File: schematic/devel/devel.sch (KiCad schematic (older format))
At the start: 61 parts, among them J1 CONN_PWR, J2 CONN_X1, J3 CONN_Y2, J4 CONN_X2, J5 CONN_Y1, Q1 Q_PMOS_GSD, Q2 Q_NMOS_GSD, Q3 Q_PMOS_GSD, Q4 Q_NMOS_GSD, U1 LM317_SOT223, U2 LM337_SOT223, U3 REF5010IDGK, U4 OPA4197

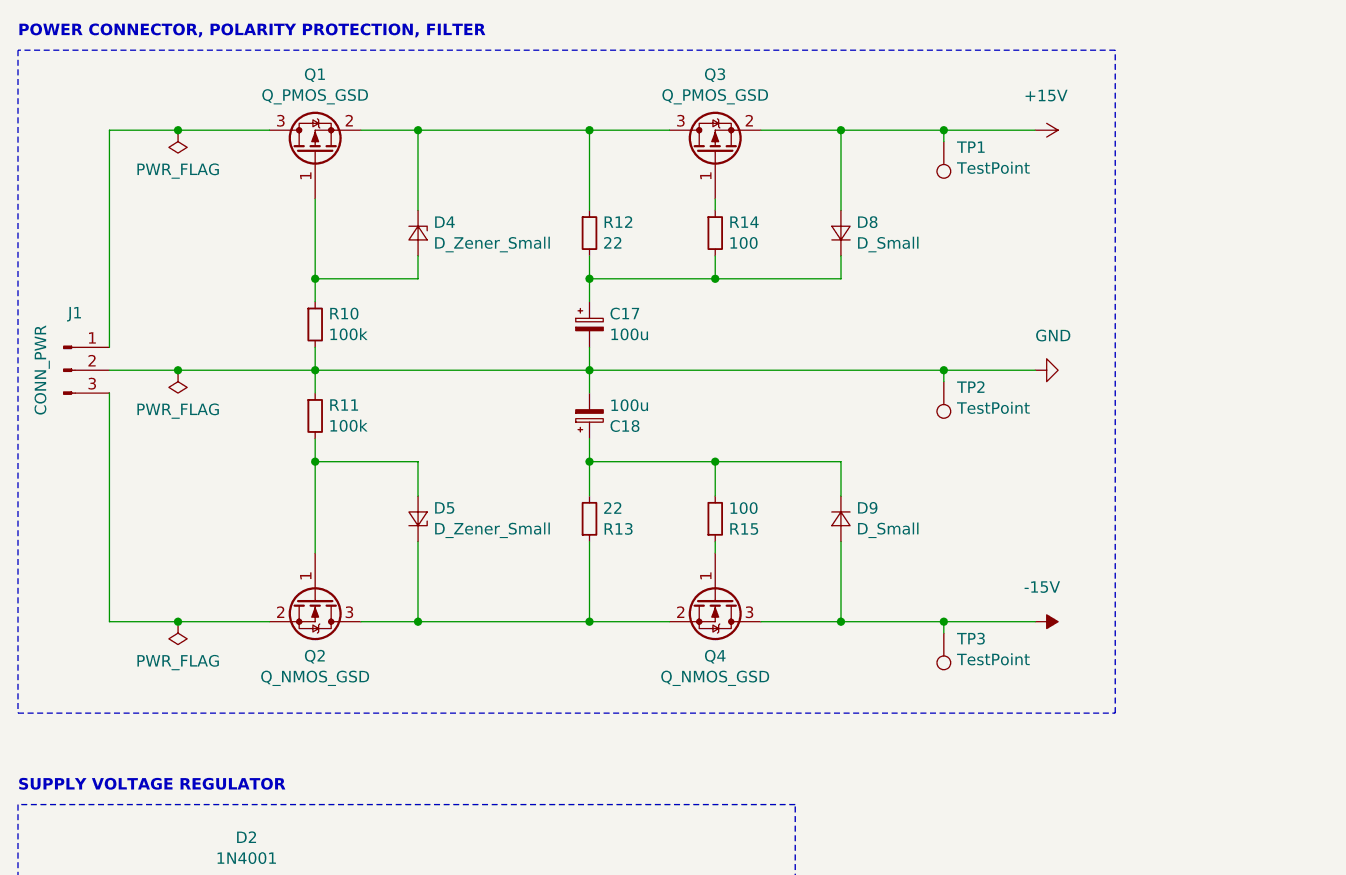
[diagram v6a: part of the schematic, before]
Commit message: completed sublayout of power input
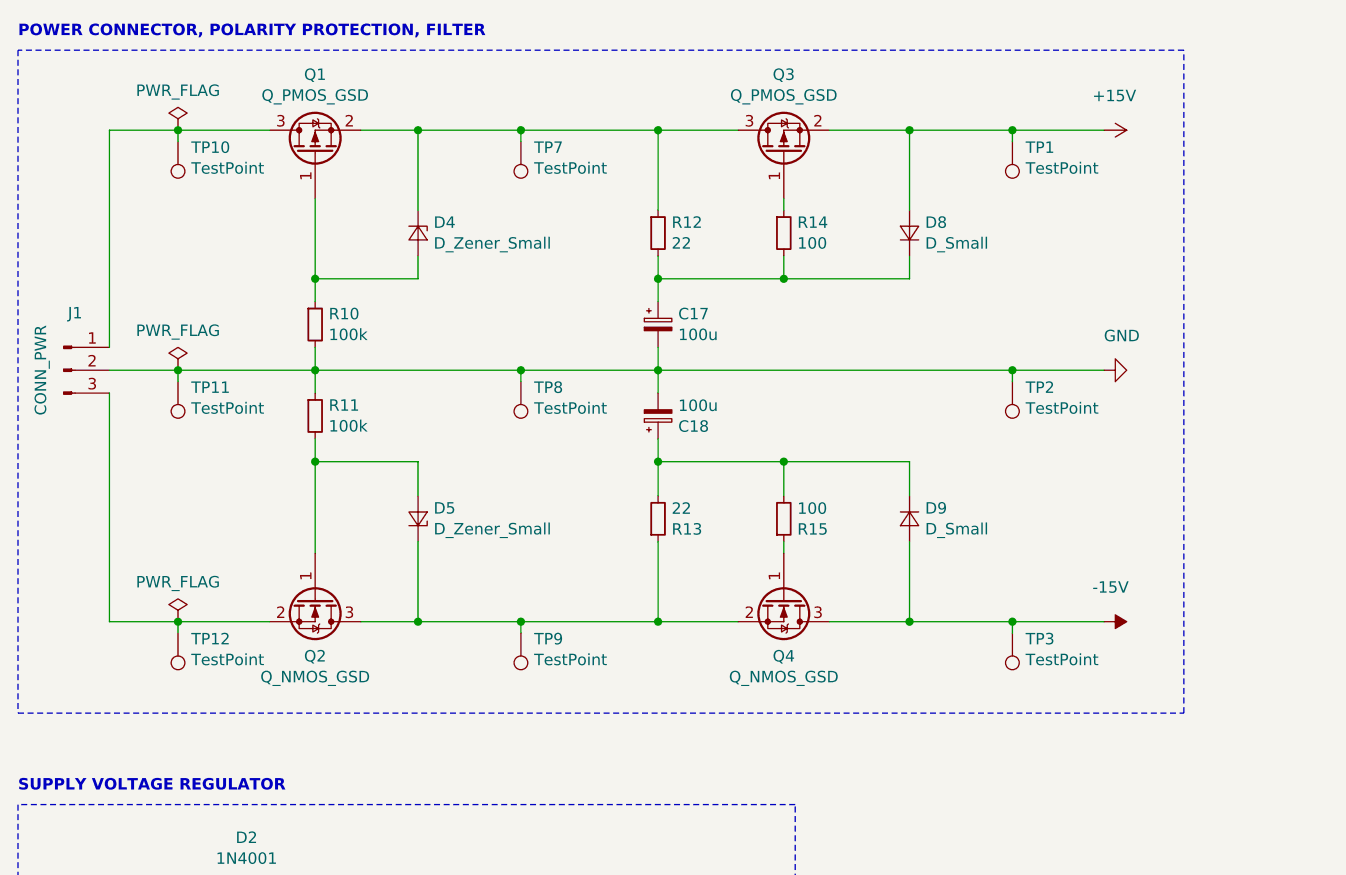
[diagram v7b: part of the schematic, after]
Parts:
- added TP10, TP11, TP12, TP7, TP8, TP9: TestPoint, TestPoint:TestPoint_Pad_D1.0mm, symbol Connector:TestPoint
- J1: footprint Connector_PinHeader_1.00mm:PinHeader_1x03_P1.00mm_Vertical_SMD_Pin1Left -> Connector_PinHeader_1.00mm:PinHeader_1x03_P1.00mm_Vertical_SMD_Pin1Right
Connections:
- net GND: now also TP11.1, TP8.1
- net at J1.1 (Pin_1), Q1.3 (D): now also TP10.1
- net at J1.3 (Pin_3), Q2.2 (S): now also TP12.1
- net at D4.1 (K), Q1.2 (S), Q3.3 (D)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: now also TP7.1
- net at D5.1 (K), Q2.3 (D), Q4.2 (S)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: now also TP9.1
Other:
- moved on the sheet: C17, C18, D8, D9, Q3, Q4, R12, R13, R14, R15, TP1, TP2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

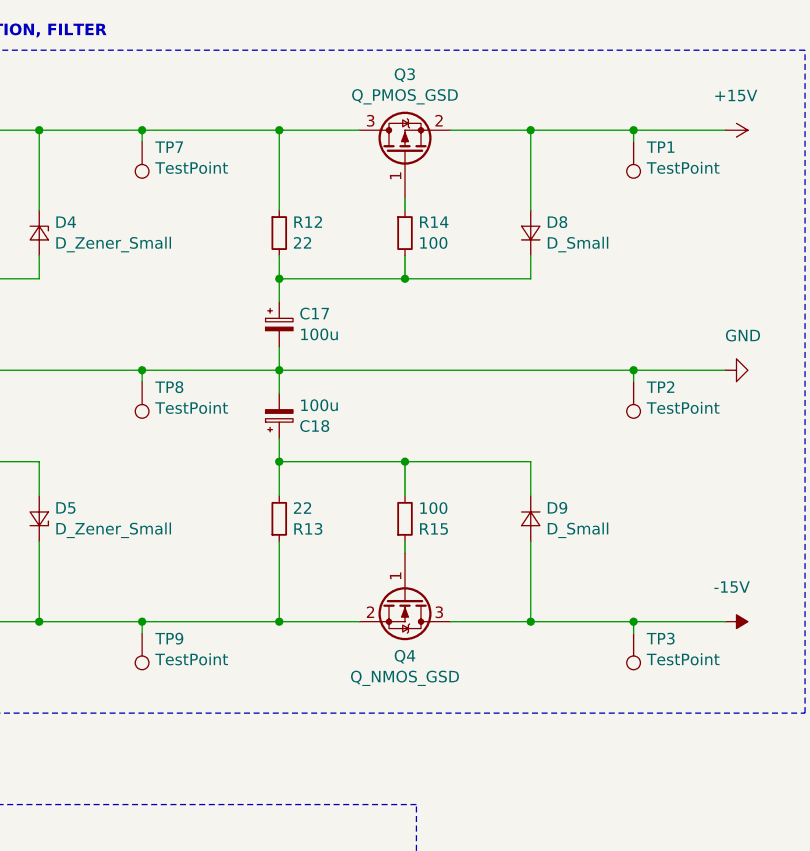
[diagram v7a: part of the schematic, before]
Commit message: created custom sma footprints
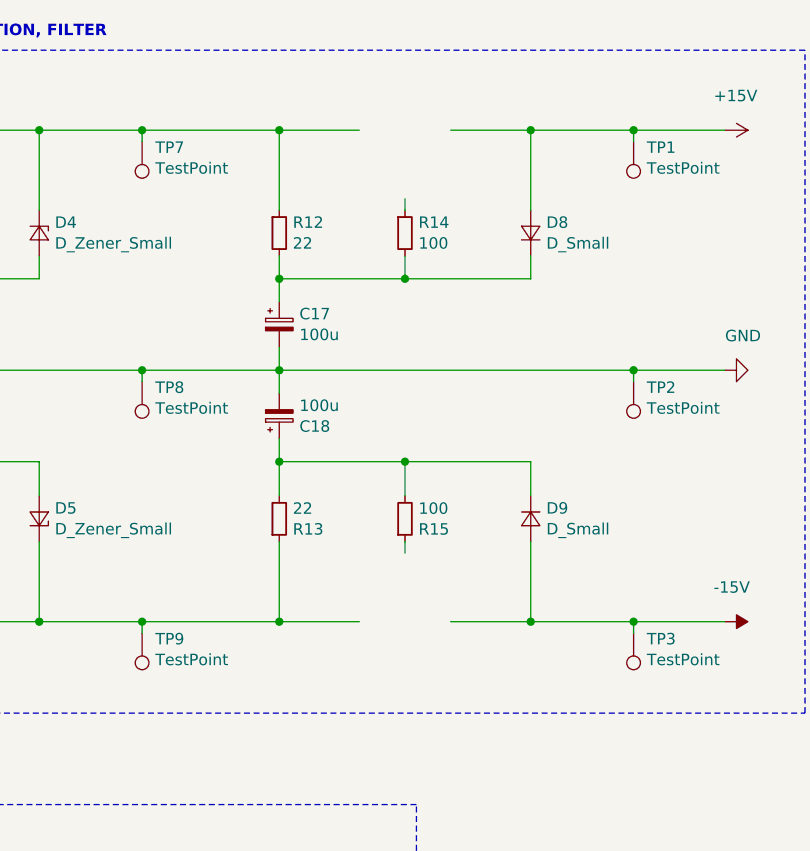
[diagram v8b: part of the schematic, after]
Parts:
- removed Q3: Q_PMOS_GSD, Package_TO_SOT_SMD:SOT-23, symbol Device:Q_PMOS_GSD
- removed Q4: Q_NMOS_GSD, Package_TO_SOT_SMD:SOT-23, symbol Device:Q_NMOS_GSD
- J2, J3, J4, J5: footprint Connector_Coaxial:SMA_Amphenol_132289_EdgeMount -> Connector_Coaxial_SMA:SMA_EdgeSlim
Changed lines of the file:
@@
 F 0 "J3" H 8850 3850 50  0000 L CNN
 F 1 "CONN_Y2" H 8700 3750 50  0000 L CNN
-F 2 "Connector_Coaxial:SMA_Amphenol_132289_EdgeMount" H 8900 3550 50  0001 C CNN
+F 2 "Connector_Coaxial_SMA:SMA_EdgeSlim" H 8900 3550 50  0001 C CNN
 F 3 " ~" H 8900 3550 50  0001 C CNN
 	1    8900 3550
@@
 F 0 "J5" H 10750 3850 50  0000 L CNN
 F 1 "CONN_Y1" H 10600 3750 50  0000 L CNN
-F 2 "Connector_Coaxial:SMA_Amphenol_132289_EdgeMount" H 10800 3550 50  0001 C CNN
+F 2 "Connector_Coaxial_SMA:SMA_EdgeSlim" H 10800 3550 50  0001 C CNN
 F 3 " ~" H 10800 3550 50  0001 C CNN
 	1    10800 3550
@@
 F 0 "J4" H 10750 2250 50  0000 L CNN
 F 1 "CONN_X2" H 10600 2150 50  0000 L CNN
-F 2 "Connector_Coaxial:SMA_Amphenol_132289_EdgeMount" H 10800 1950 50  0001 C CNN
+F 2 "Connector_Coaxial_SMA:SMA_EdgeSlim" H 10800 1950 50  0001 C CNN
 F 3 " ~" H 10800 1950 50  0001 C CNN
 	1    10800 1950
@@
 F 0 "J2" H 8850 2250 50  0000 L CNN
 F 1 "CONN_X1" H 8700 2150 50  0000 L CNN
-F 2 "Connector_Coaxial:SMA_Amphenol_132289_EdgeMount" H 8900 1950 50  0001 C CNN
+F 2 "Connector_Coaxial_SMA:SMA_EdgeSlim" H 8900 1950 50  0001 C CNN
 F 3 " ~" H 8900 1950 50  0001 C CNN
 	1    8900 1950
@@
 Wire Wire Line
 	3450 1450 3450 1100
-$Comp
-L Device:Q_PMOS_GSD Q3
-U 1 1 5D5D688A
-P 4000 1200
-F 0 "Q3" V 4343 1200 50  0000 C CNN
-F 1 "Q_PMOS_GSD" V 4252 1200 50  0000 C CNN
-F 2 "Package_TO_SOT_SMD:SOT-23" H 4200 1300 50  0001 C CNN
-F 3 "~" H 4000 1200 50  0001 C CNN
-	1    4000 1200
-	0    -1   -1   0
-$EndComp
 Wire Wire Line
 	4200 1100 4550 1100
@@
 Wire Wire Line
 	4550 3250 5000 3250
-$Comp
-L Device:Q_NMOS_GSD Q4
-U 1 1 5D6EB887
-P 4000 3150
-F 0 "Q4" V 4251 3150 50  0000 C CNN
-F 1 "Q_NMOS_GSD" V 4342 3150 50  0000 C CNN
-F 2 "Package_TO_SOT_SMD:SOT-23" H 4200 3250 50  0001 C CNN
-F 3 "~" H 4000 3150 50  0001 C CNN
-	1    4000 3150
-	0    1    1    0
-$EndComp
 Wire Wire Line
 	4200 3250 4550 3250
